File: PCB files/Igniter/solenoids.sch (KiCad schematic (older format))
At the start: 33 parts, among them Q2 N MOSFET, Q3 N MOSFET, Q4 N MOSFET, Q5 N MOSFET, Q6 N MOSFET, U2 FDS8984, U3 FDS8984, U4 FDS8984

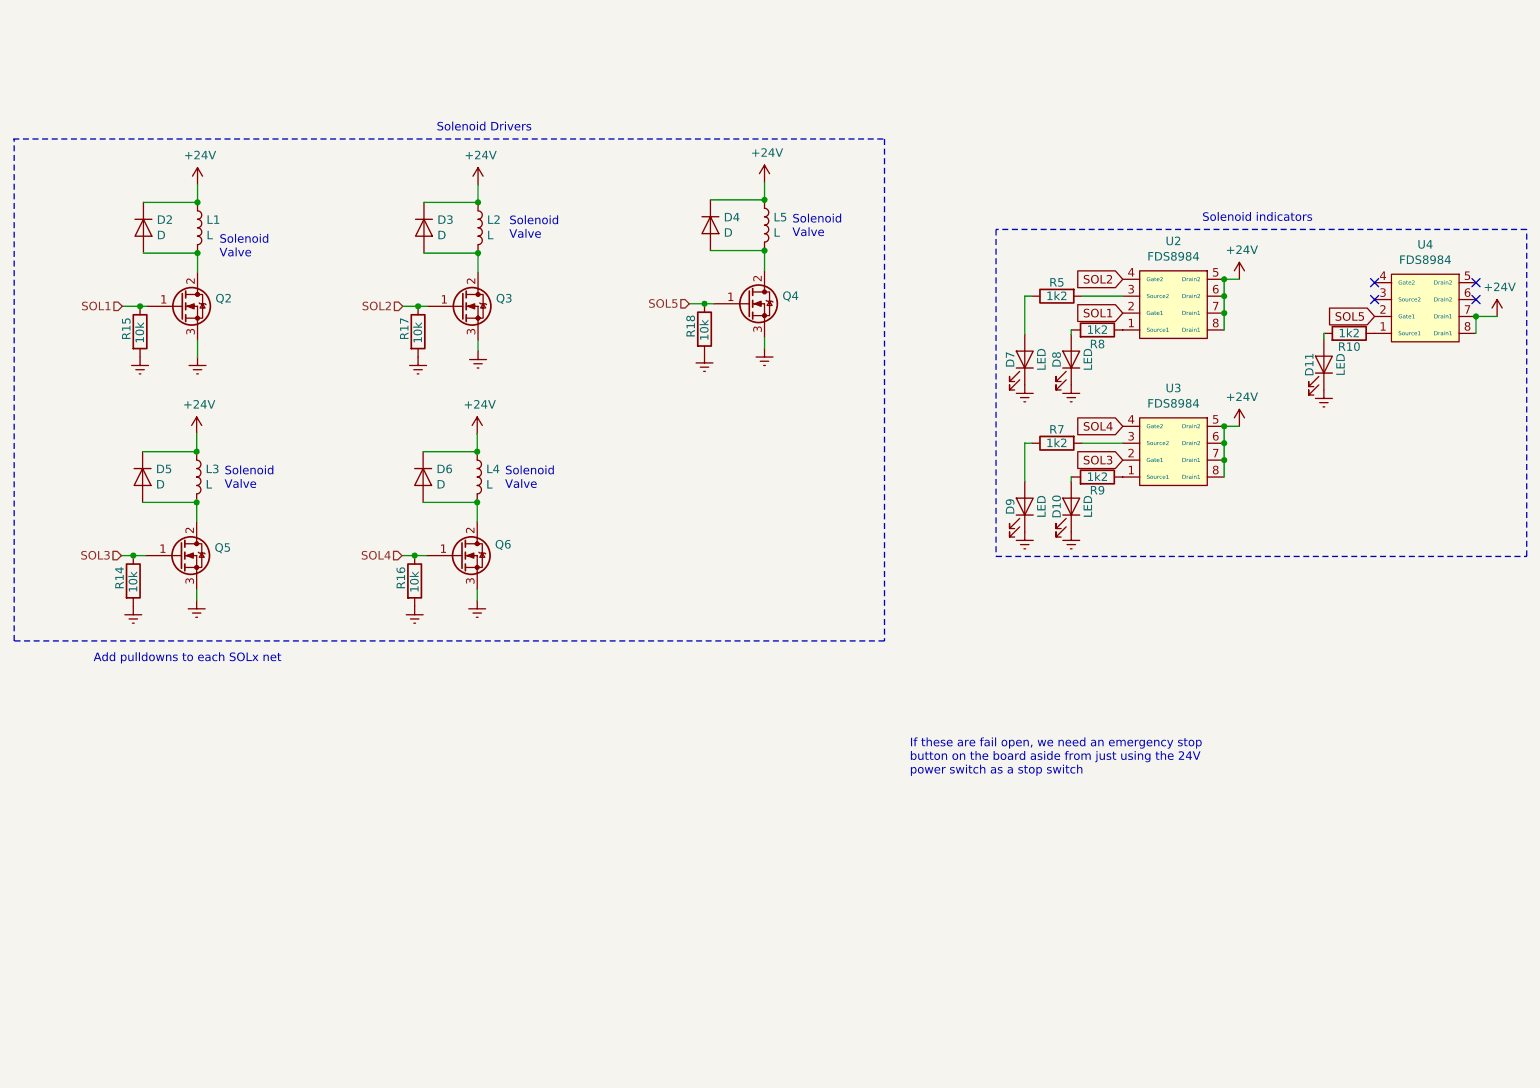
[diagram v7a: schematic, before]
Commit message: 12/4/2019
-Changed solenoids to dsub connection
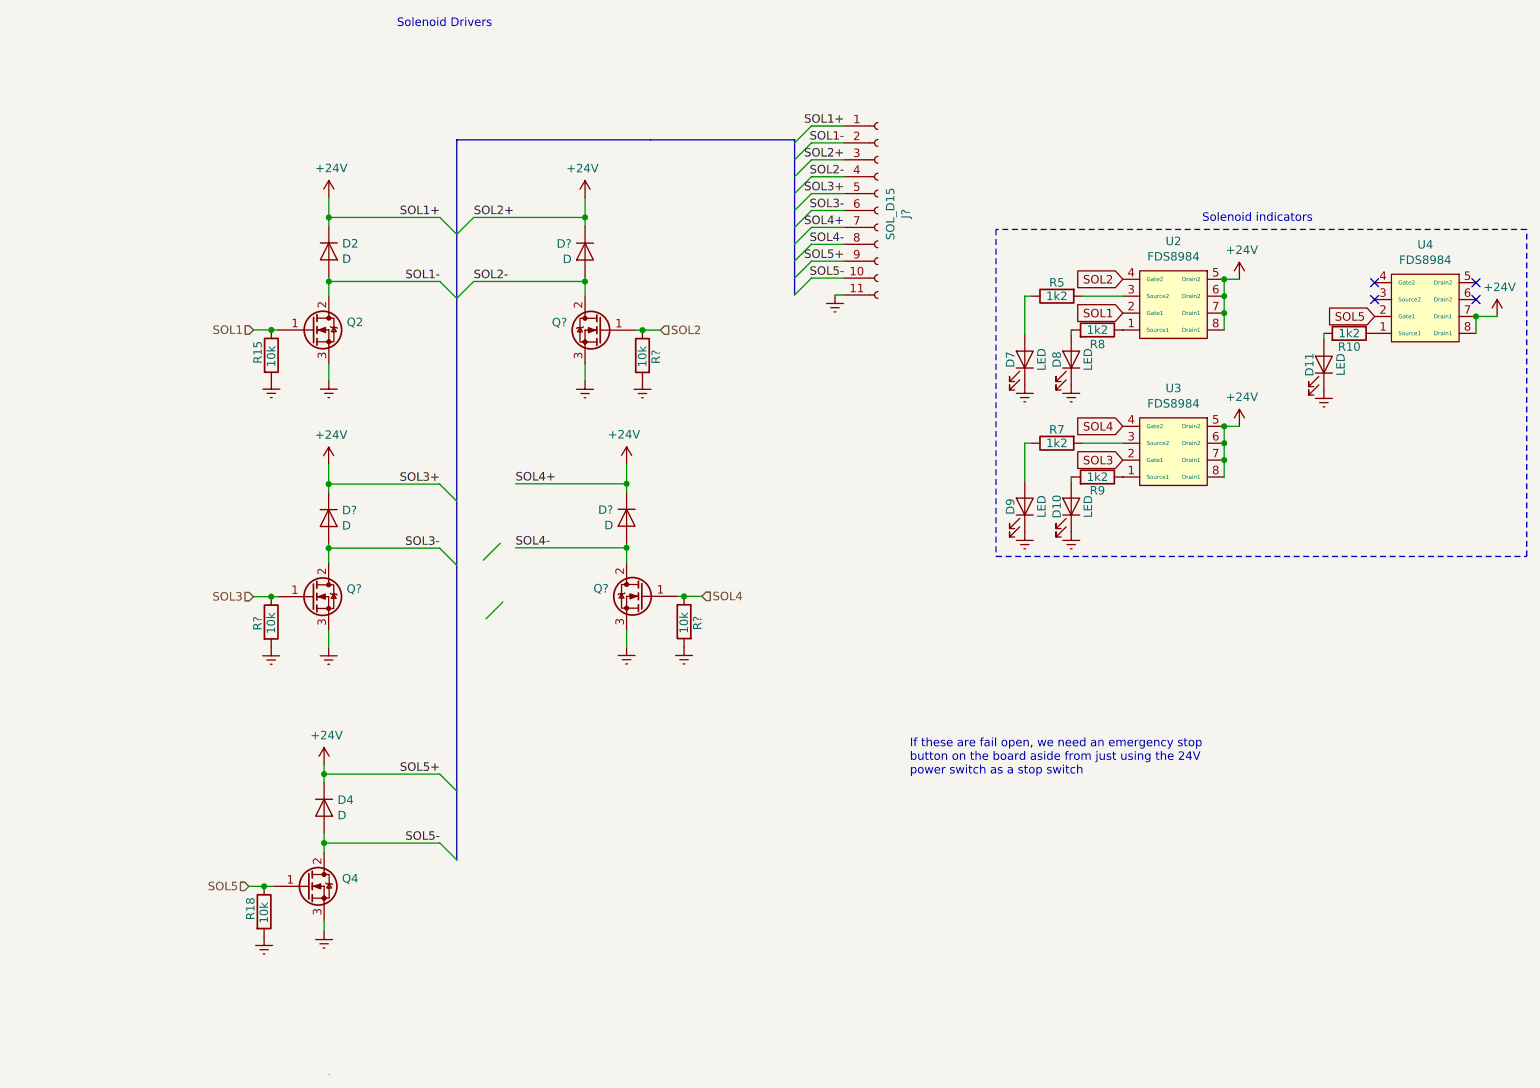
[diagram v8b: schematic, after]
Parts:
- removed D3, D5, D6: D, Diode_SMD:D_SOD-123F, symbol Device:D
- removed L1, L2, L3, L4, L5: L, Connector_Molex:Molex_Mini-Fit_Jr_5566-04A_2x02_P4.20mm_Vertical, symbol Device:L
- removed Q3, Q5, Q6: N MOSFET, Package_TO_SOT_SMD:SOT-223, symbol Device:Q_NMOS_GDS
- removed R14, R16, R17: 10k, Resistor_SMD:R_1206_3216Metric, symbol Device:R
- added D? (x3): D, Diode_SMD:D_SOD-123F, symbol Device:D
- added J?: SOL_D15, symbol Connector:Conn_01x11_Female
- added Q? (x3): N MOSFET, Package_TO_SOT_SMD:SOT-223, symbol Device:Q_NMOS_GDS
- added R? (x3): 10k, Resistor_SMD:R_1206_3216Metric, symbol Device:R
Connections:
- net +24V: now also D?.1 (K), D?.1 (K), D?.1 (K), J?.1 (Pin_1), J?.3 (Pin_3), J?.5 (Pin_5), J?.7 (Pin_7), J?.9 (Pin_9)
- net GNDREF: now also J?.11 (Pin_11), Q?.3 (S), Q?.3 (S), Q?.3 (S), R?.2, R?.2, R?.2
- net SOL2: now also Q?.1 (G), R?.1
- net SOL3: now also Q?.1 (G), R?.1
- net SOL4: now also Q?.1 (G), R?.1
- net SOL1-: now reaches D2.2 (A), Q2.2 (D)
- net SOL1-: now also J?.2 (Pin_2)
- net SOL5-: now reaches D4.2 (A), Q4.2 (D)
- net SOL5-: now also J?.10 (Pin_10)
- new net SOL2-: D?.2 (A), J?.4 (Pin_4), Q?.2 (D)
- new net SOL3-: D?.2 (A), J?.6 (Pin_6), Q?.2 (D)
- new net SOL4-: D?.2 (A), J?.8 (Pin_8), Q?.2 (D)
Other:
- note removed: "Add pulldowns to each SOLx net"
- note removed: "Solenoid\nValve"
- moved on the sheet: D2, D4, Q2, Q4, R15, R18
